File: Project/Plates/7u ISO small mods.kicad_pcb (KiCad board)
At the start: 2 copper layers, 257.2 x 76.2 mm, 43 parts

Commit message: pcb & plate revisions & firmware
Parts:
- removed the REF** at (146.1, 91.3)
- added REF**: Value, cipulot_parts:ecs_plate_cut_7U_space_stab, F.Cu at (146.1, 91.3)
- added REF**: Value, cipulot_parts:ecs_7U_space_stab, F.Cu at (146.1, 91.3)

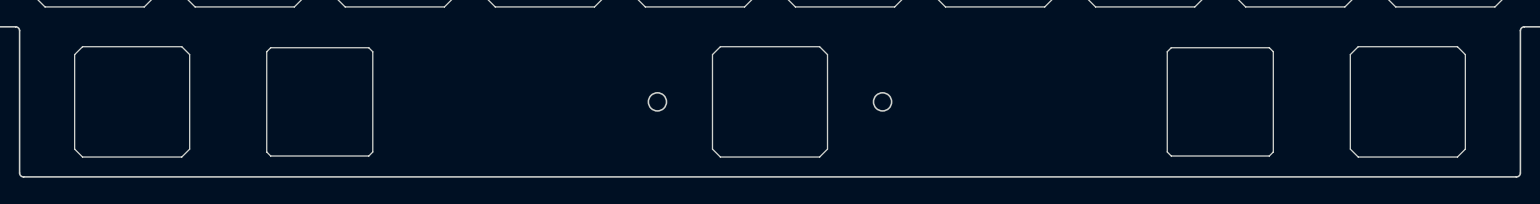
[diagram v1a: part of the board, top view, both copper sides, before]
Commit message: bottom row change, plate update, firmware update
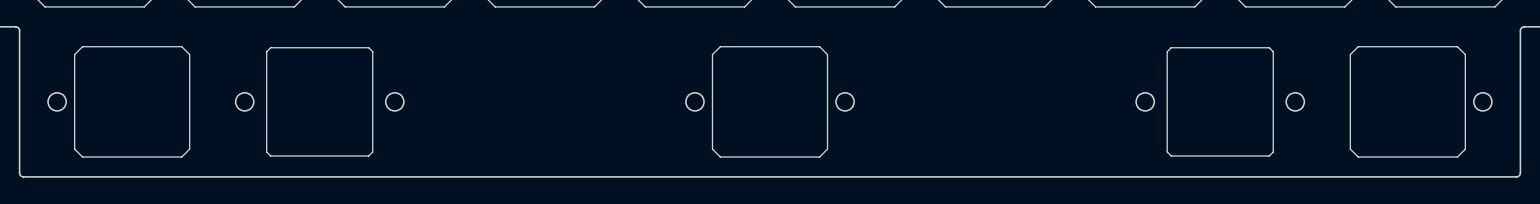
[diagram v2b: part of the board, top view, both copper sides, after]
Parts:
- removed the REF** at (146.1, 91.3)
- added REF**: Value, cipulot_parts:ecs_6U_space_stab, F.Cu at (146.1, 91.3)
- turned REF** to 0 degrees
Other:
- outline, holes or cut-outs redrawn
- board text added: "REF**"
